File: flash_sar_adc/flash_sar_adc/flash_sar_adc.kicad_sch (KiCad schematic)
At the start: 57 parts, among them J1 Conn_02x06_Matched, J2 Conn_02x06_Matched, U1 LM339DR, U2 LM339DR, U3 OPA843xDBV, U4 SPX3819M5-L-3-0

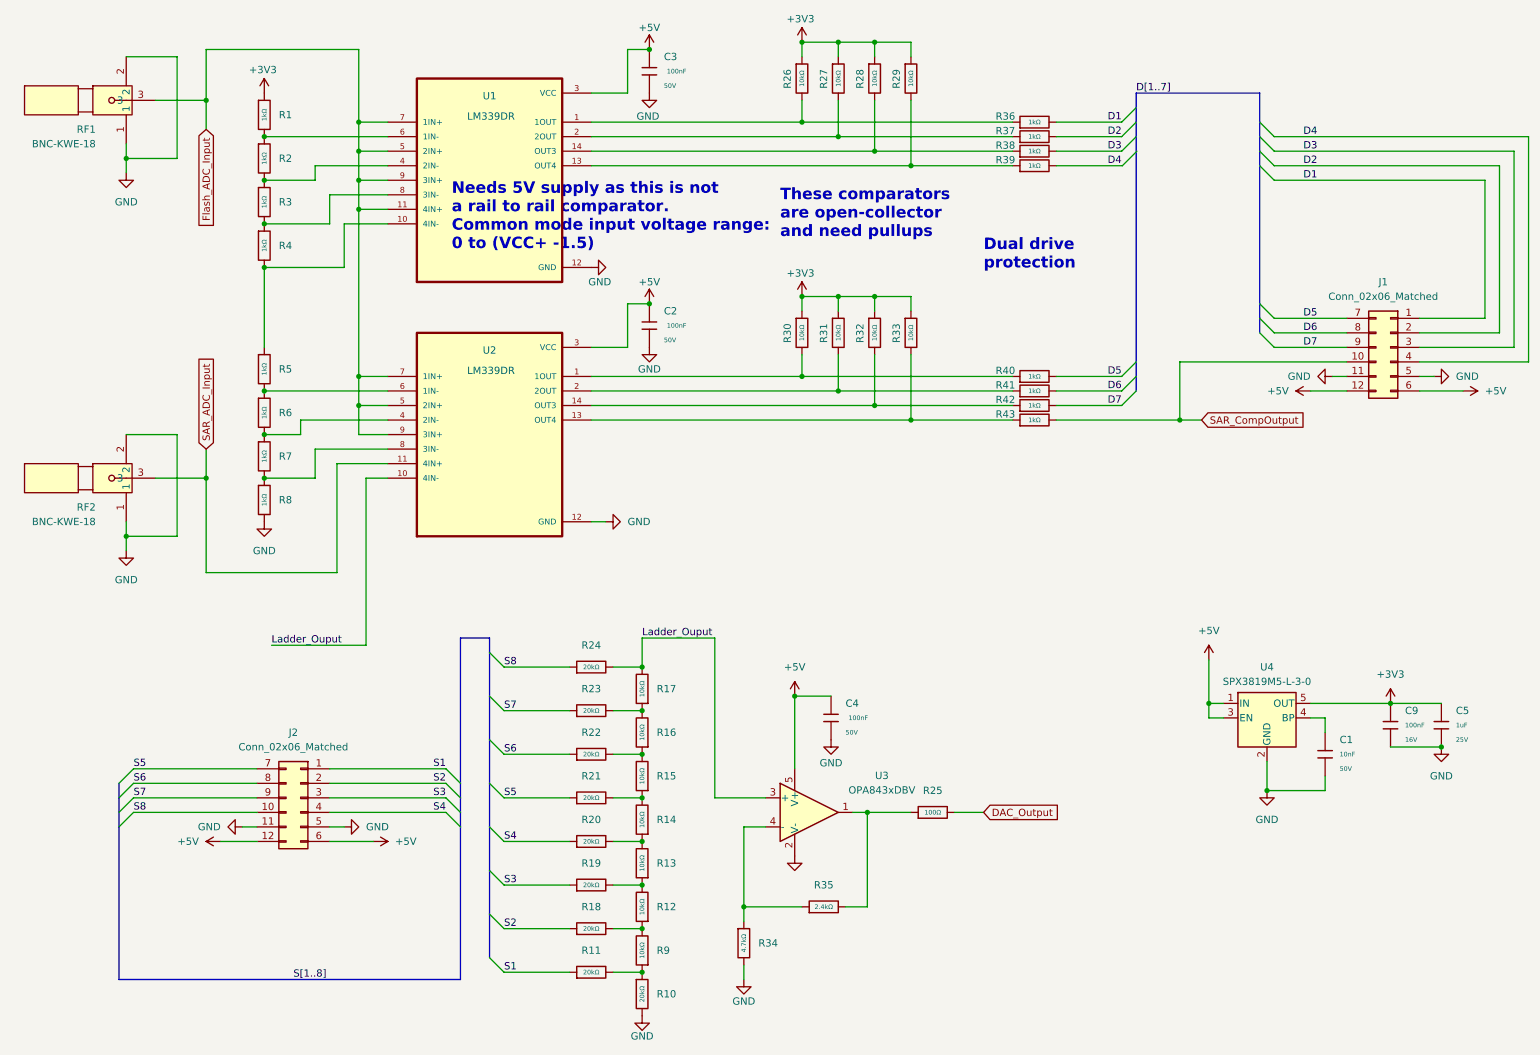
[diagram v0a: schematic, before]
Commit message: added Test Points
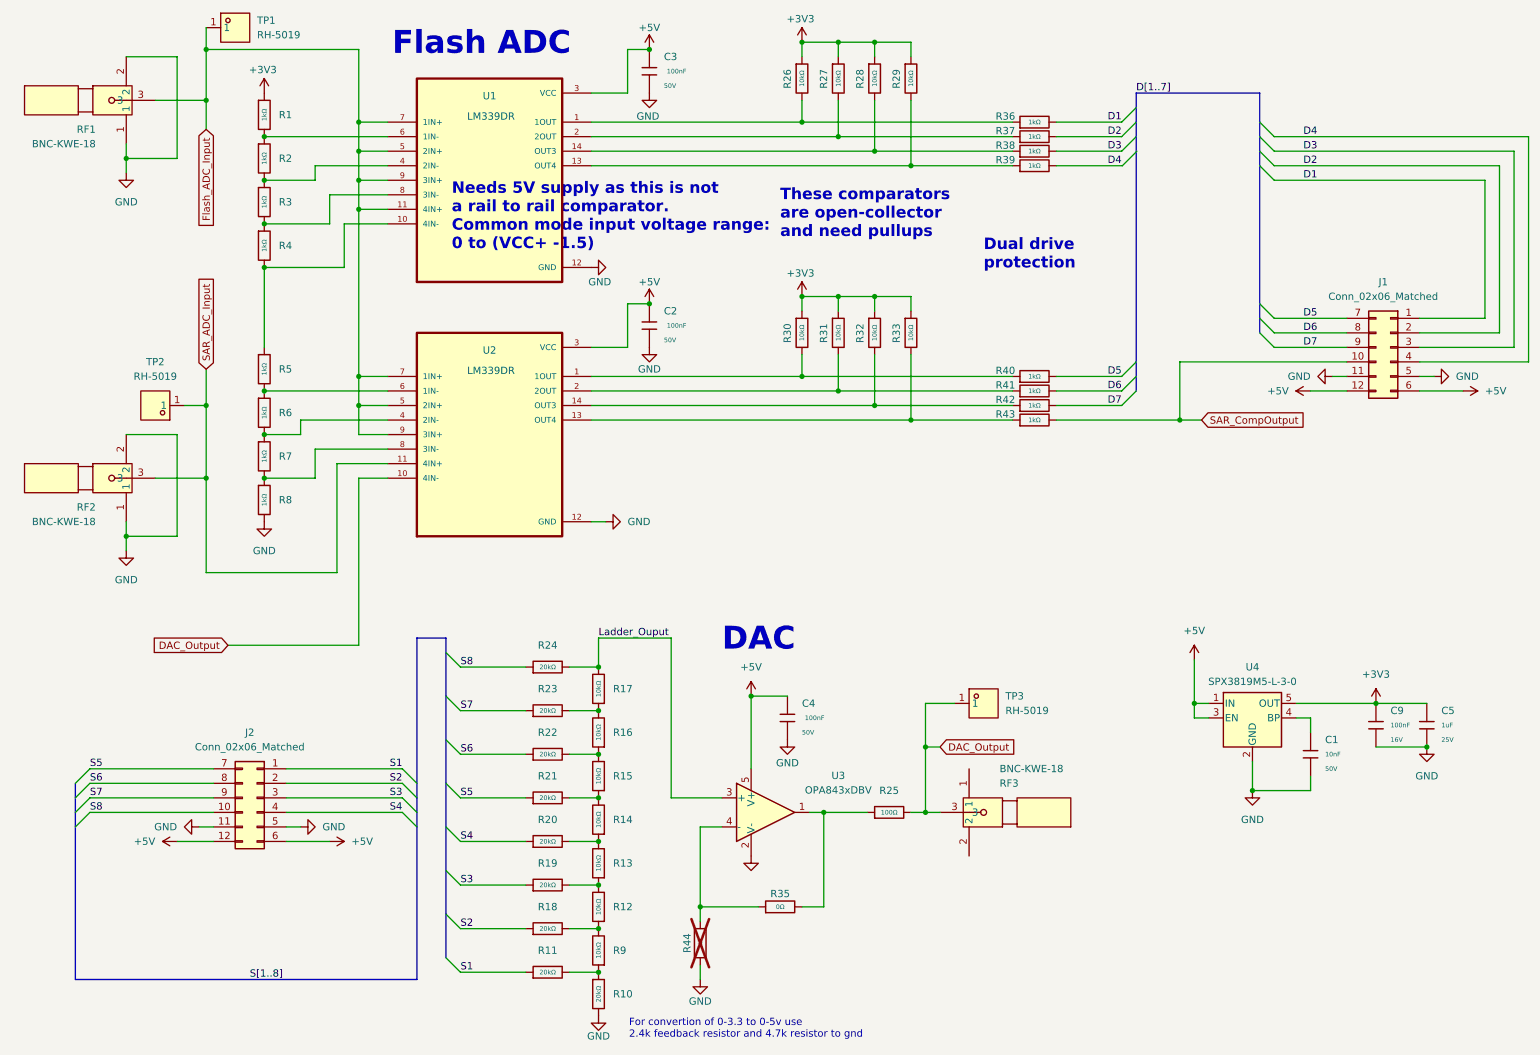
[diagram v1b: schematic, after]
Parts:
- removed R34: 4.7kΩ, PCM_JLCPCB:R_0402, symbol PCM_JLCPCB-Resistors:0402,4.7kΩ
- removed R35: 2.4kΩ, PCM_JLCPCB:R_0402, symbol PCM_JLCPCB-Resistors:0402,2.4kΩ
- added R35: 0Ω, PCM_JLCPCB:R_0402, symbol PCM_JLCPCB-Resistors:0402,0Ω
- added R44: NA, PCM_JLCPCB:R_0402, symbol PCM_JLCPCB-Resistors:0402,0Ω
- added RF3: BNC-KWE-18, BNC:SMA-TH_BNC-KWE-18, symbol BNC:BNC-KWE-18
- added TP1, TP2, TP3: RH-5019, Test Point:TESTPOINT-SMD_L3.8-W2.0_RH-5019, symbol Test Point:RH-5019
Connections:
- net DAC_Output: now also U2.10 (4IN-), RF3.3, TP3.1
- net Flash_ADC_Input: now also TP1.1
- net GND: now also R44.1
- net Ladder_Ouput: no longer U2.10 (4IN-)
- net SAR_ADC_Input: now also TP2.1
- net at U3.4 (-): now also R35.1, R44.2
- net at R25.1, U3.1: now also R35.2
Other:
- note added: "DAC"
- note added: "Flash ADC"
- note added: "For convertion of 0-3.3 to 0-5v use 2.4k feedback resistor and 4.7k resistor to gnd"
- moved on the sheet: C1, C4, C5, C9, J2, R10, R11, R12, R13, R14, R15, R16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

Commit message: finished flash/sar adc board
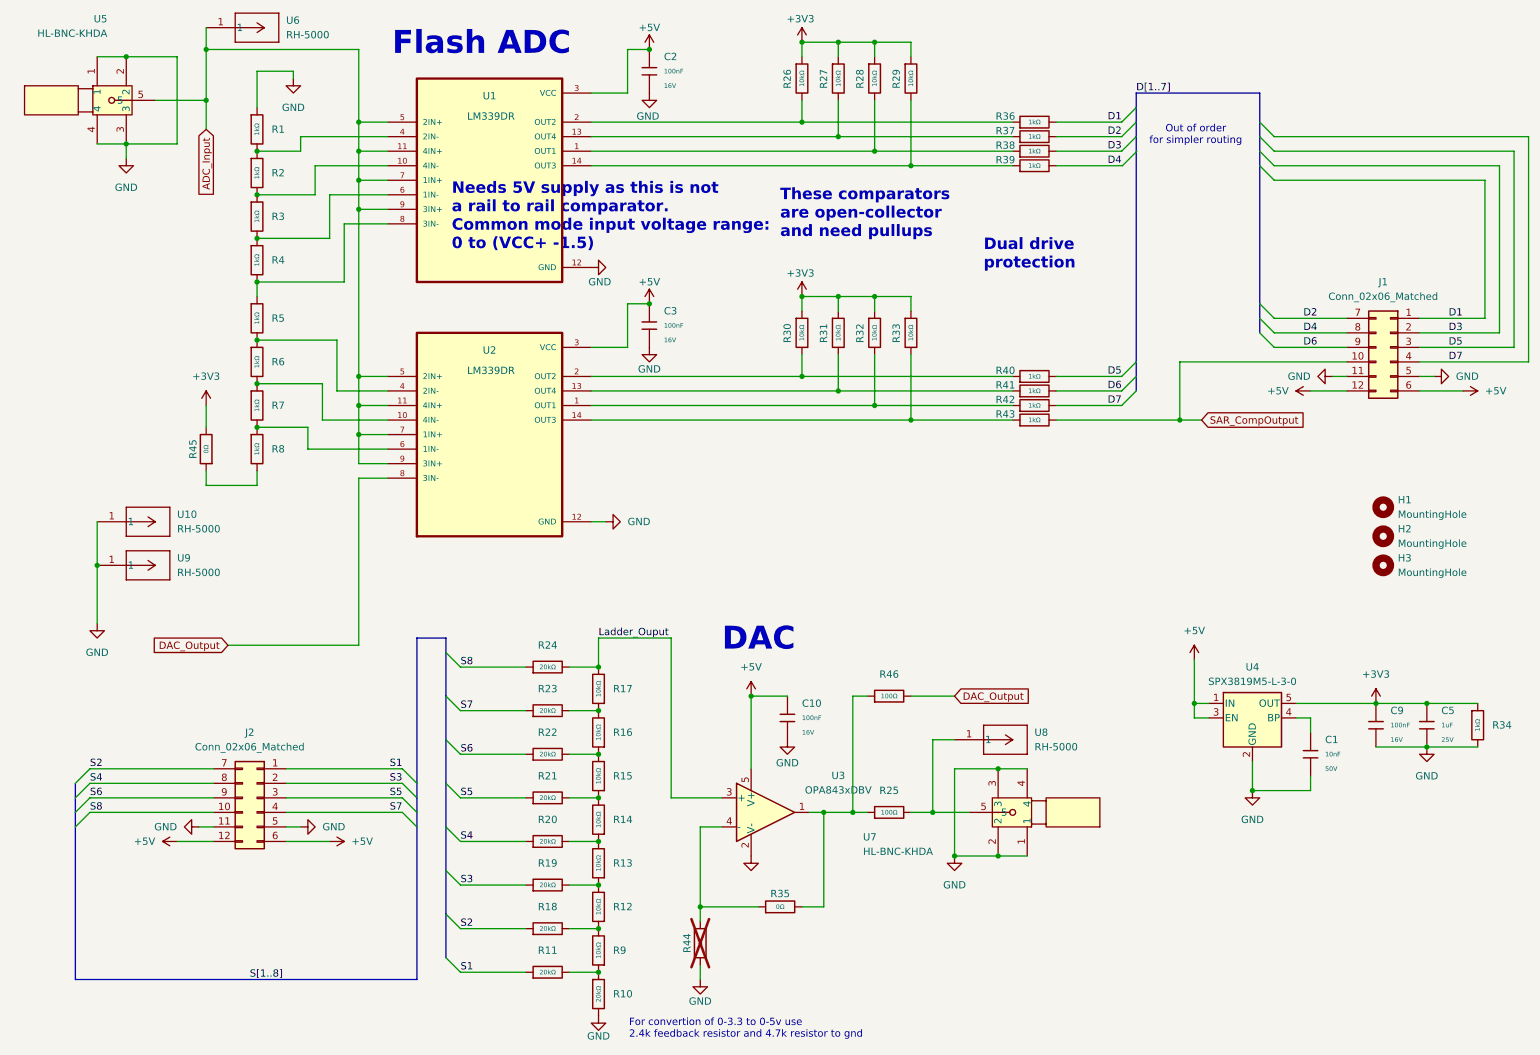
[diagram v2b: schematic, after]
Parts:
- removed C2, C3, C4: 100nF, PCM_JLCPCB:C_0603, symbol PCM_JLCPCB-Capacitors:0603,100nF
- removed RF1, RF2, RF3: BNC-KWE-18, BNC:SMA-TH_BNC-KWE-18, symbol BNC:BNC-KWE-18
- removed TP1, TP2, TP3: RH-5019, Test Point:TESTPOINT-SMD_L3.8-W2.0_RH-5019, symbol Test Point:RH-5019
- added C10, C2, C3: 100nF, PCM_JLCPCB:C_0402, symbol PCM_JLCPCB-Capacitors:0402,100nF
- added H1, H2, H3: MountingHole, MountingHole:MountingHole_3.5mm, symbol Mechanical:MountingHole
- added R34: 1kΩ, PCM_JLCPCB:R_0402, symbol PCM_JLCPCB-Resistors:0402,1kΩ
- added R45: 0Ω, PCM_JLCPCB:R_0402, symbol PCM_JLCPCB-Resistors:0402,0Ω
- added R46: 100Ω, PCM_JLCPCB:R_0402, symbol PCM_JLCPCB-Resistors:0402,100Ω
- added U10, U6, U8, U9: RH-5000, Test Point:CONN1_1514-2_KEY, symbol Test Point:534-1514-2
- added U5, U7: HL-BNC-KHDA, easyeda:BNC-TH_L12.0-W12.0, symbol easyeda:HL-BNC-KHDA
- J1, J2: LCSC (none) -> C5383091
- U1, U2: footprint LM339DR:SOIC127P600X175-14N -> comp footprint:SOIC127P600X175-14N
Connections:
- net SAR_ADC_Input is gone; now on net ADC_Input: U2.11 (4IN+)
- net +3V3: now also R34.1, R45.2; no longer R1.1
- net +5V: now also C10.1, C2.1, C3.1
- net D2: now also J1.7 (Pin_7); no longer J1.2 (Pin_2)
- net D3: now also J1.2 (Pin_2); no longer J1.3 (Pin_3)
- net D4: now also J1.8 (Pin_8); no longer J1.4 (Pin_4)
- net D5: now also J1.3 (Pin_3); no longer J1.7 (Pin_7)
- net D6: now also J1.9 (Pin_9); no longer J1.8 (Pin_8)
- net D7: now also J1.4 (Pin_4); no longer J1.9 (Pin_9)
- net DAC_Output: now also U2.8 (3IN-), R46.2; no longer R25.2, U2.10 (4IN-)
- net GND: now also R1.1, C10.2, C2.2, C3.2, R34.2, U10.1, U5.1, U5.2, U5.3, U5.4, U7.1, U7.2, U7.3, U7.4, U9.1; no longer R8.2
- net S2: now also J2.7 (Pin_7); no longer J2.2 (Pin_2)
- net S3: now also J2.2 (Pin_2); no longer J2.3 (Pin_3)
- net S4: now also J2.8 (Pin_8); no longer J2.4 (Pin_4)
- net S5: now also J2.3 (Pin_3); no longer J2.7 (Pin_7)
- net S6: now also J2.9 (Pin_9); no longer J2.8 (Pin_8)
- net S7: now also J2.4 (Pin_4); no longer J2.9 (Pin_9)
- net at R30.2, R40.1: now also U2.2 (OUT2); no longer U2.1 (1OUT)
- net at R27.2, R37.1: now also U1.13 (OUT4); no longer U1.2 (2OUT)
- net at R26.2, R36.1: now also U1.2 (OUT2); no longer U1.1 (1OUT)
- net at R4.2, R5.1: now also U1.8 (3IN-); no longer U1.10 (4IN-)
- net at R29.2, R39.1: now also U1.14 (OUT3); no longer U1.13 (OUT4)
- net at R28.2, R38.1: now also U1.1 (OUT1); no longer U1.14 (OUT3)
- net at R2.2, R3.1: now also U1.10 (4IN-); no longer U1.4 (2IN-)
- net at R1.2, R2.1: now also U1.4 (2IN-); no longer U1.6 (1IN-)
- net at R3.2, R4.1: now also U1.6 (1IN-); no longer U1.8 (3IN-)
- net at R33.2, R43.1: now also U2.14 (OUT3); no longer U2.13 (OUT4)
- net at R32.2, R42.1: now also U2.1 (OUT1); no longer U2.14 (OUT3)
- net at R7.2, R8.1: now also U2.6 (1IN-); no longer U2.8 (3IN-)
- net at R31.2, R41.1: now also U2.13 (OUT4); no longer U2.2 (2OUT)
- net at R6.2, R7.1: now also U2.10 (4IN-); no longer U2.4 (2IN-)
- net at R5.2, R6.1: now also U2.4 (2IN-); no longer U2.6 (1IN-)
- net at R25.1, R35.2, U3.1: now also R46.1
- net Flash_ADC_Input renamed ADC_Input
- net ADC_Input: now also U5.5, U6.1
- new net: R25.2, U7.5, U8.1
- new net: R45.1, R8.2
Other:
- note added: "Out of order for simpler routing"

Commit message: fixed power supply errors
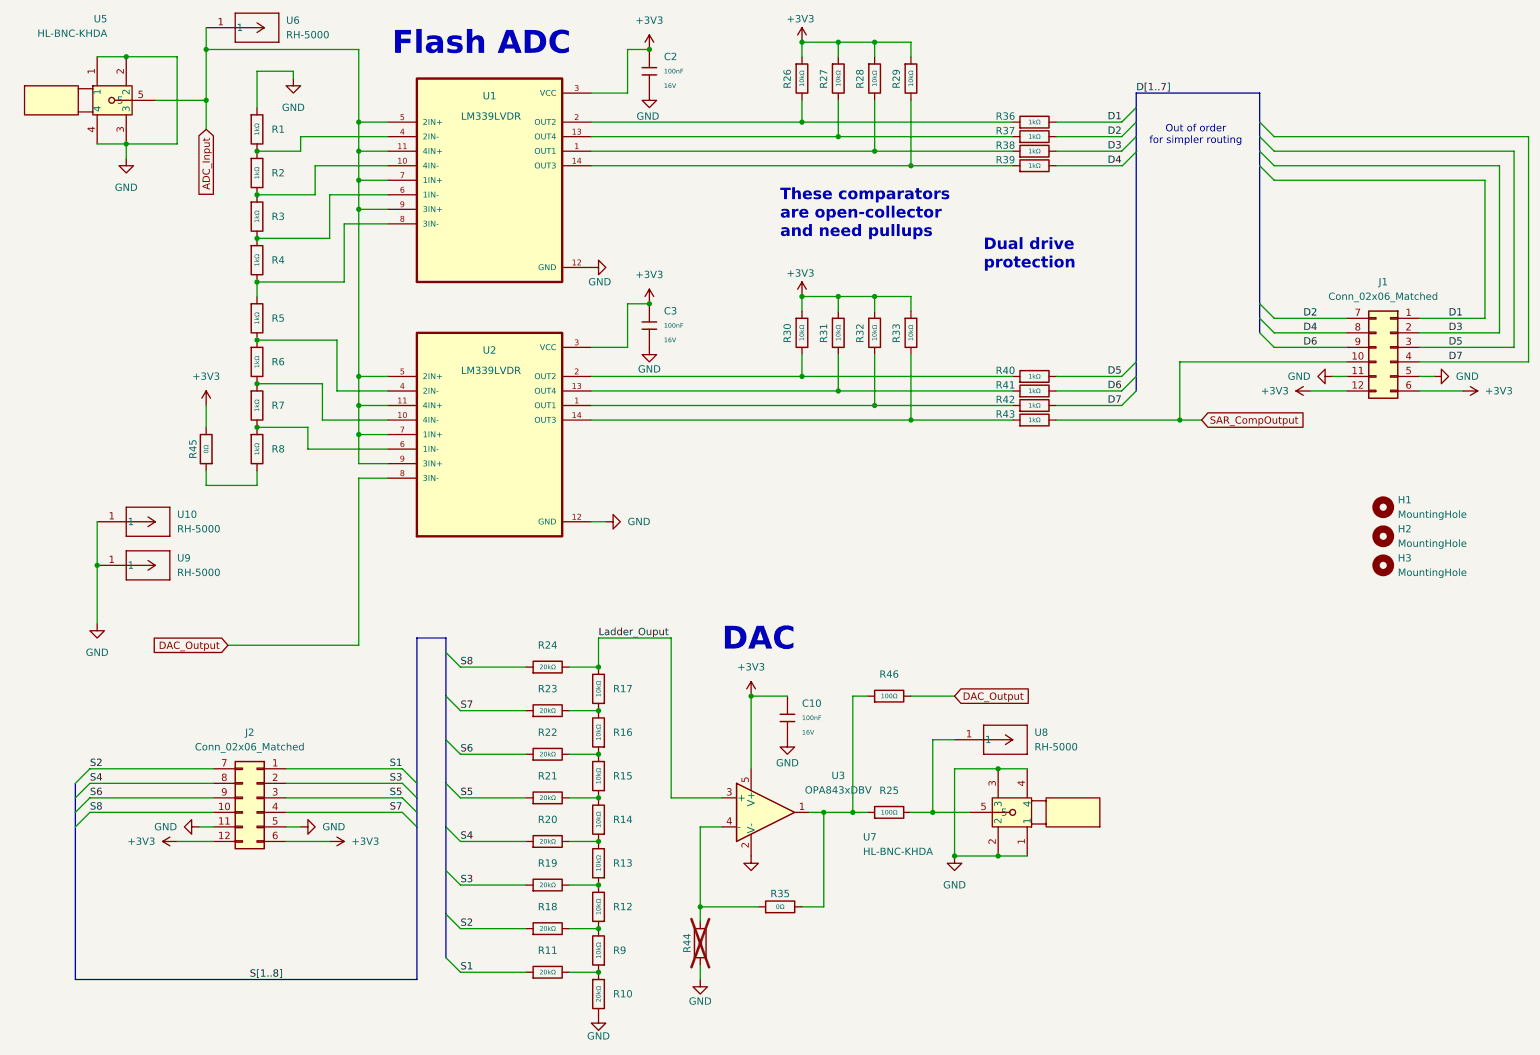
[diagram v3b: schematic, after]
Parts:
- removed C1: 10nF, PCM_JLCPCB:C_0402, symbol PCM_JLCPCB-Capacitors:0402,10nF
- removed C5: 1uF, PCM_JLCPCB:C_0402, symbol PCM_JLCPCB-Capacitors:0402,1uF
- removed C9: 100nF, PCM_JLCPCB:C_0402, symbol PCM_JLCPCB-Capacitors:0402,100nF
- removed R34: 1kΩ, PCM_JLCPCB:R_0402, symbol PCM_JLCPCB-Resistors:0402,1kΩ
- removed U4: SPX3819M5-L-3-0, Package_TO_SOT_SMD:SOT-23-5, symbol Regulator_Linear:SPX3819M5-L-3-0
- U1: value LM339DR -> LM339LVDR
- U2: value LM339DR -> LM339LVDR; LCSC C5236695 -> C22427665
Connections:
- net +5V is gone; now on net +3V3: C10.1, C2.1, C3.1, J1.12 (Pin_12), J1.6 (Pin_6), J2.12 (Pin_12), J2.6 (Pin_6), U1.3 (VCC), U2.3 (VCC), U3.5 (V+)
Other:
- note removed: "For convertion of 0-3.3 to 0-5v use 2.4k feedback resistor and 4.7k resistor to gnd"
- note removed: "Needs 5V supply as this is not a rail to rail comparator. Common mode input voltage range: 0 to (VCC+ -1.5)"

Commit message: fixed bom errors
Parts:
- U1: LCSC C5236695 -> C22427665
- U10, U6, U8, U9: now left out of the parts list
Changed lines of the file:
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@@
 		(polyline
 			(pts
-				(xy 180.34 22.86) (xy 200.66 22.86) (xy 200.66 95.25) (xy 180.34 95.25)
+				(xy 13.97 119.38) (xy 204.47 119.38) (xy 204.47 165.1) (xy 167.64 165.1) (xy 167.64 196.85) (xy 13.97 196.85)
 			)
 			(stroke
@@
 		(polyline
 			(pts
-				(xy 146.05 16.51) (xy 177.8 16.51) (xy 177.8 97.79) (xy 146.05 97.79)
+				(xy 180.34 22.86) (xy 200.66 22.86) (xy 200.66 95.25) (xy 180.34 95.25)
 			)
 			(stroke
@@
 		(polyline
 			(pts
-				(xy 13.97 119.38) (xy 204.47 119.38) (xy 204.47 165.1) (xy 167.64 165.1) (xy 167.64 196.85) (xy 13.97 196.85)
+				(xy 146.05 16.51) (xy 177.8 16.51) (xy 177.8 97.79) (xy 146.05 97.79)
 			)
 			(stroke
@@
 			)
 		)
-		(property "Description" "25nA 4 SOP-14 Linear Comparators RoHS"
+		(property "Description" "5pA Four channels SOIC-14 Linear Comparators RoHS"
 			(at 96.52 44.45 0)
 			(effects
@@
 			)
 		)
-		(property "LCSC" "C5236695"
+		(property "LCSC" "C22427665"
 			(at 96.52 44.45 0)
 			(effects
@@
 		(unit 1)
 		(exclude_from_sim no)
-		(in_bom yes)
+		(in_bom no)
 		(on_board yes)
 		(dnp no)
@@
 		(unit 1)
 		(exclude_from_sim no)
-		(in_bom yes)
+		(in_bom no)
 		(on_board yes)
 		(dnp no)
@@
 			)
 		)
-		(property "Description" "25nA Four channels SOP-14 Linear Comparators RoHS"
+		(property "Description" "5pA Four channels SOIC-14 Linear Comparators RoHS"
 			(at 96.52 88.9 0)
 			(effects
@@
 		(unit 1)
 		(exclude_from_sim no)
-		(in_bom yes)
+		(in_bom no)
 		(on_board yes)
 		(dnp no)
@@
 		(unit 1)
 		(exclude_from_sim no)
-		(in_bom yes)
+		(in_bom no)
 		(on_board yes)
 		(dnp no)
